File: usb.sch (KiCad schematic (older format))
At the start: 10 parts

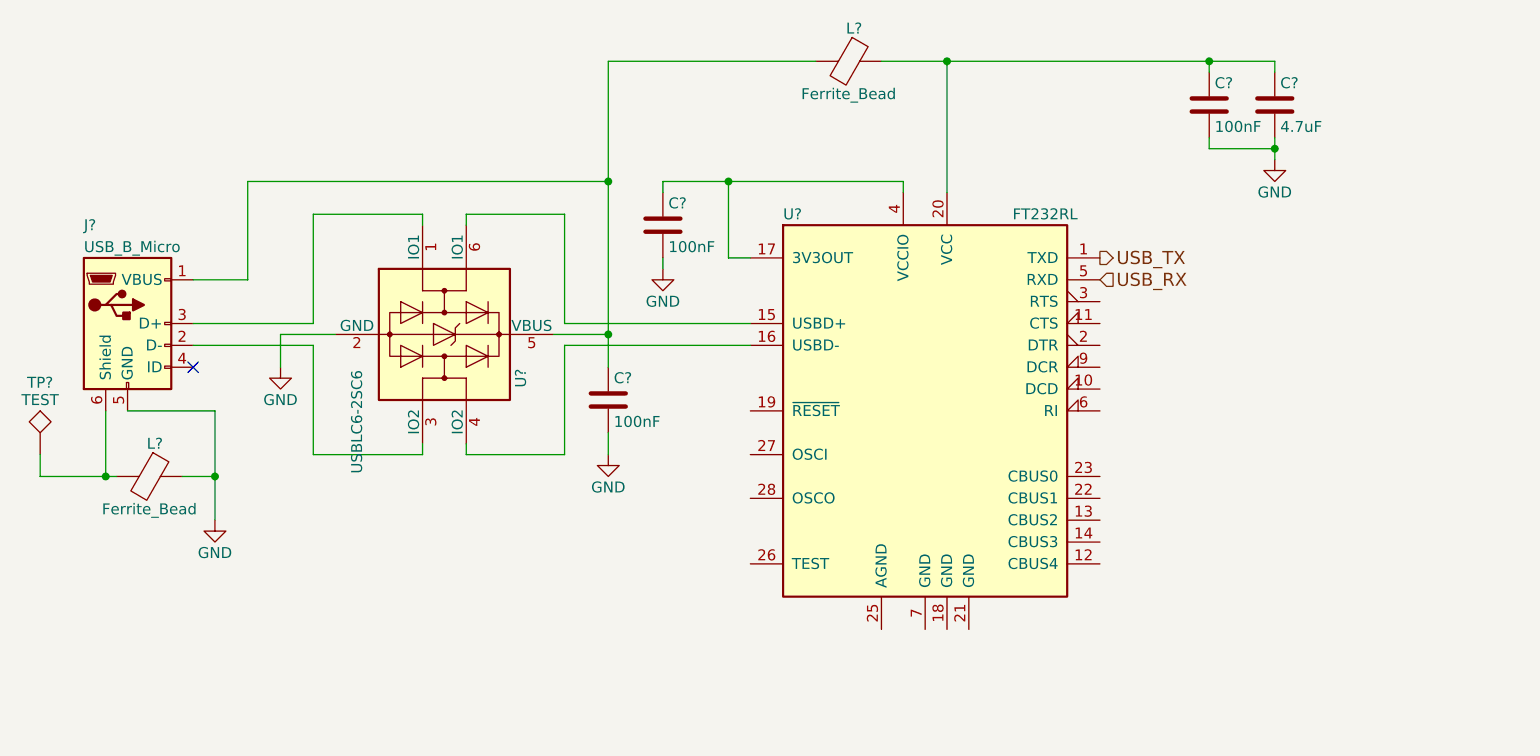
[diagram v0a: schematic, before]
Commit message: Remove redundant global power labels
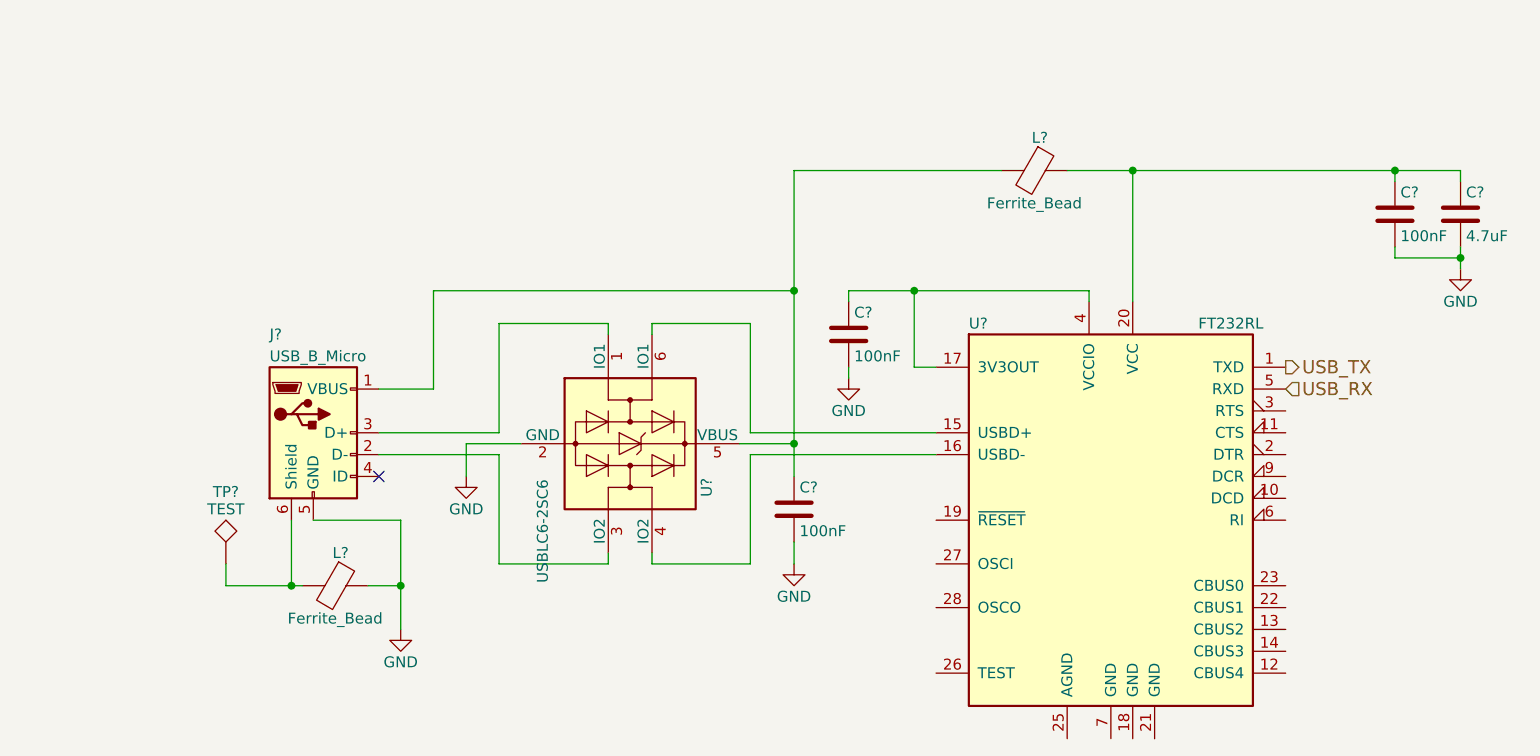
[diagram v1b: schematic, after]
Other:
- moved on the sheet: C?, J?, L?, TP?, U?
